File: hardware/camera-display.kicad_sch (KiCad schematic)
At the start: 6 parts, among them J3 ILI9341 Display Module, J4 OV2640 Camera Module, Q1 2N7002

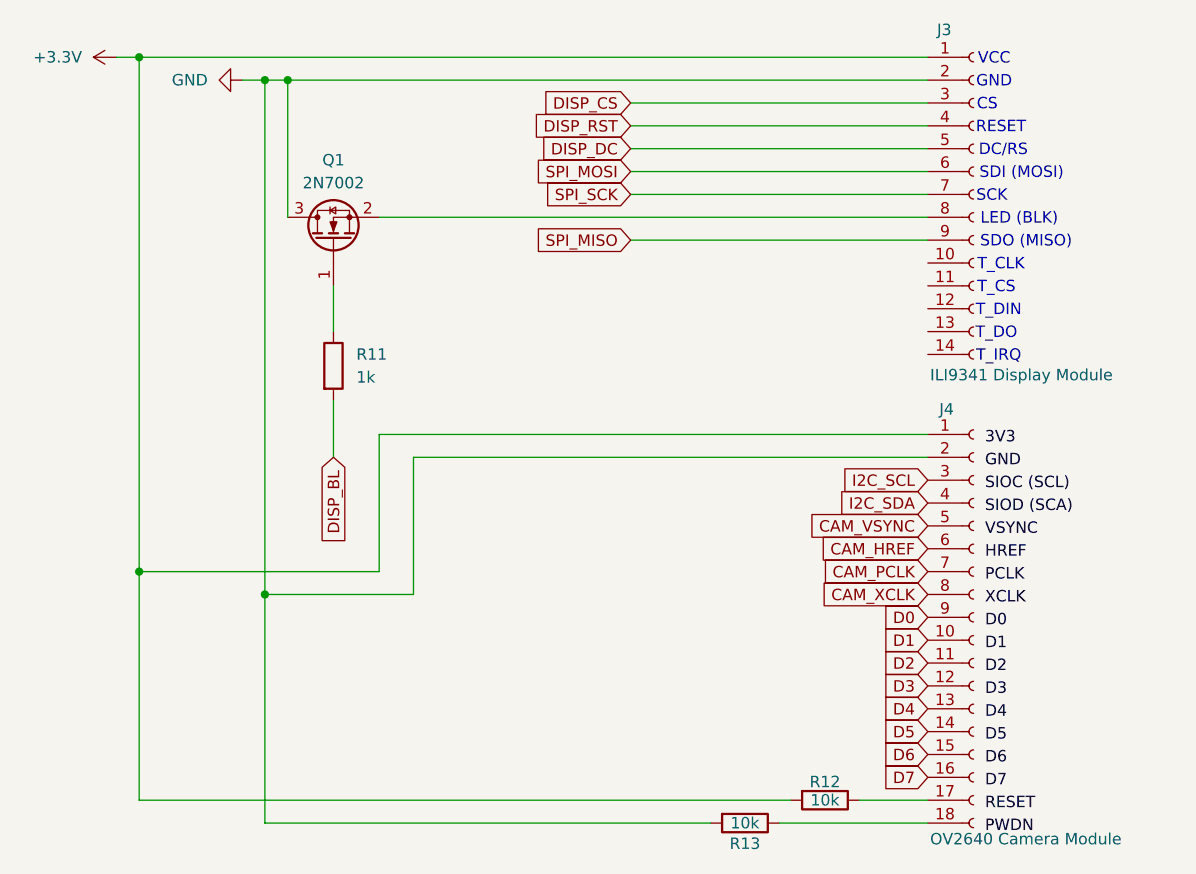
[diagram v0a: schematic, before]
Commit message: all design sheets complete, ERC clean
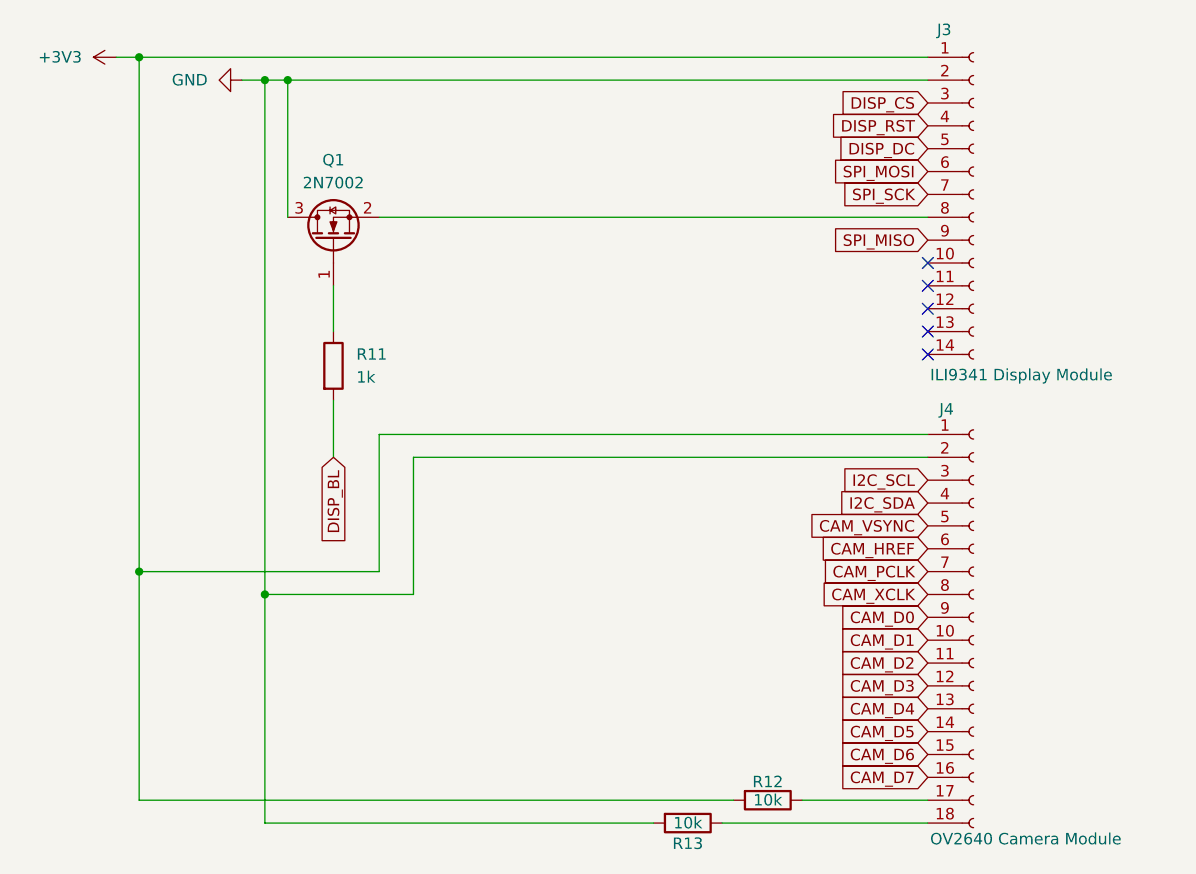
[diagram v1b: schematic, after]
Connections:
- net +3.3V renamed +3V3
- net D0 renamed CAM_D0
- net D1 renamed CAM_D1
- net D2 renamed CAM_D2
- net D3 renamed CAM_D3
- net D4 renamed CAM_D4
- net D5 renamed CAM_D5
- net D6 renamed CAM_D6
- net D7 renamed CAM_D7
- no-connect marks 0 -> 5
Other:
- note removed: "CS"
- note removed: "DC/RS"
- note removed: "GND"
- note removed: "LED (BLK)"
- note removed: "RESET"
- note removed: "SCK"
- note removed: "SDI (MOSI)"
- note removed: "SDO (MISO)"
- note removed: "T_CLK"
- note removed: "T_CS"
- note removed: "T_DIN"
- note removed: "T_DO"
- note removed: "T_IRQ"
- note removed: "VCC"
- moved on the sheet: R12, R13
